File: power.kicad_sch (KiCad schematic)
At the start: 35 parts, among them J1 OBD-II harness, U1 TLV431A

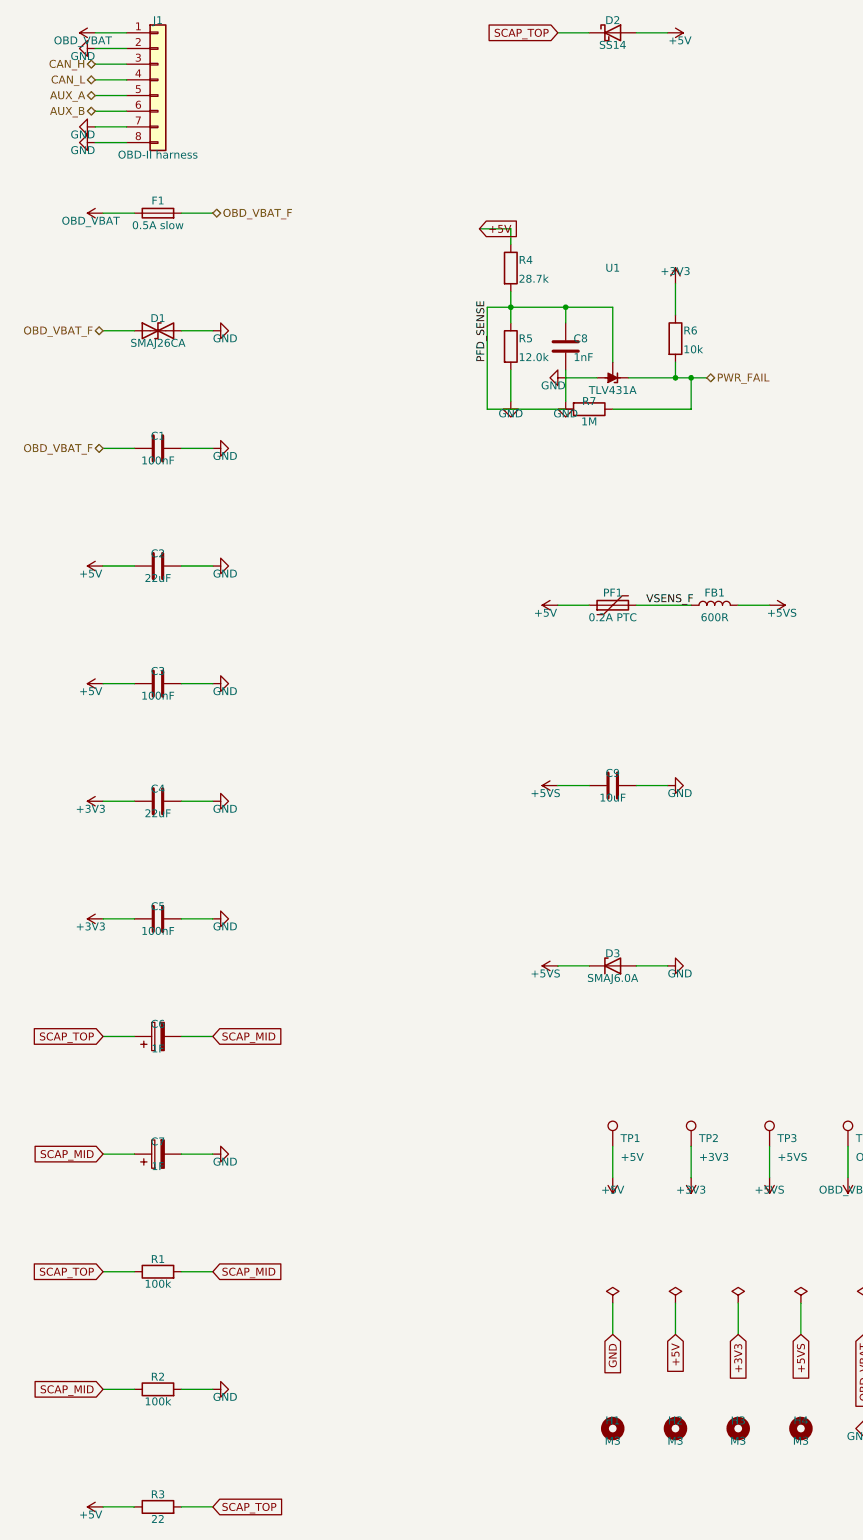
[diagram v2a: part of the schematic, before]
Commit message: Route, audit and document the carrier; verify every part number against the catalogue
Ordering is the point of this pass, so the part numbers came first. Every
LCSC number on the board was opened and read -- manufacturer part, package,
and the parameter that decides whether it is the right part. That found:

  C2148396 for the MCP2518FD    is an 18.7k resistor, out of stock -> C626759
  C255909  for a 40 MHz crystal is a 16 MHz crystal              -> C5186937
  C157966  for a JST PH 10-way  is a JST XH 9-way, 2.5 mm pitch  -> C158038

Three of the five numbers introduced last sitting were wrong, and all three
were plausible enough that the BOM exported clean. docs/PARTS.md records the
lot, including that LCSC's own listing for the microSD socket claims it has
no card-detect switch -- it has one, and the schematic is right.

Two footprints would not have soldered: both polyfuses are 1812 parts sitting
on a 1206 land, inherited from the parent board where nothing had ever
compared a part's package against its footprint. And the generic-passive
table was keyed on value alone, so the 1206 positions added last sitting
would have ordered 0805 parts -- right resistance, wrong footprint, every
board. It is keyed on (value, package) now and returns nothing rather than
guessing, so an unmatched line has no part number and somebody has to look.

Several values moved to match what is actually stocked: the power-fail
divider to 43k/18k (same trip point to 2 mV, both stocked 1 % parts), the
K-line series and pull-up to 20 R and 750 R, and the supercap charge resistor
from 22 R to 100 R -- 22 R put 1 W into a 250 mW part for the first several
seconds of every power-up.

Two real defects, both found by tools rather than by reading:

  - The hold-up Schottky was BACKWARDS. Reversed it shorts out the inrush
    limiter and blocks the discharge, so the supercap bank could never hold
    the rail up and the whole hold-up circuit was inert. audit_polarity found
    it once its expectat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
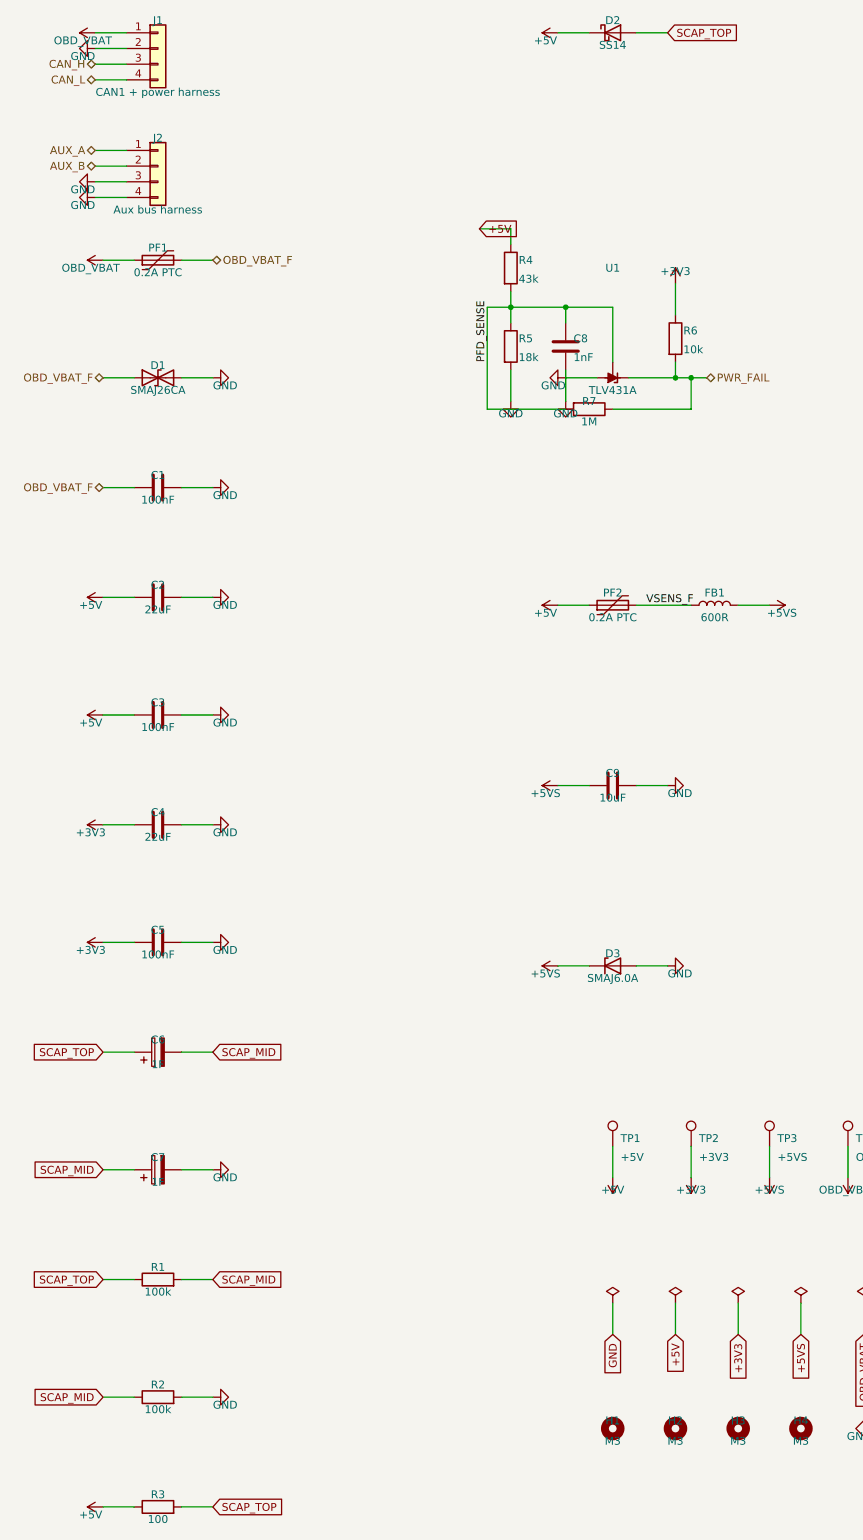
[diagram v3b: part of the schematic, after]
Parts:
- removed F1: 0.5A slow, Fuse:Fuse_1206_3216Metric, symbol Device:Fuse
- added J2: Aux bus harness, Connector_JST:JST_PH_B4B-PH-K_1x04_P2.00mm_Vertical, symbol Connector_Generic:Conn_01x04
- added PF2: 0.2A PTC, Resistor_SMD:R_1812_4532Metric, symbol Device:Polyfuse
- D2: Note Discharge path, bypassing the charge resistor. Anode on the bank: it conducts only once the rail has sagged a diode drop below the bank, which is exactly when the supply has gone away -> Discharge path, bypassing the charge resistor. Anode on the bank, cathode on the rail: it conducts only once the rail has sagged a diode drop below the bank, which is exactly when the supply has gone away
- J1: value OBD-II harness -> CAN1 + power harness; footprint Connector_JST:JST_PH_B8B-PH-K_1x08_P2.00mm_Vertical -> Connector_JST:JST_PH_B4B-PH-K_1x04_P2.00mm_Vertical; symbol Connector_Generic:Conn_01x08 -> Connector_Generic:Conn_01x04; MPN JST B8B-PH-K-S(LF)(SN) -> JST B4B-PH-K-S(LF)(SN); Note Pins 3/4 are the first CAN bus, always. Pins 5/6 are the se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 -> OBD-II pins 16/4/6/14. Pin 1 is sense only -- the board is 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
- PF1: footprint Resistor_SMD:R_1206_3216Metric -> Resistor_SMD:R_1812_4532Metric; MPN Bourns MF-MSMF020 -> Bourns MF-MSMF020/60-2; Note Resettable: a shorted sensor wire trips this, not the dev b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 -> OBD-II pin 16 is PERMANENT battery -- live with the ignitio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
- R3: value 22 -> 100; Note Inrush limit. 1206 for the pulse rating: 210 mA into 22 ohm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 -> Inrush limit, and the value is set by the resistor's own ra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
- R4: value 28.7k -> 43k
- R5: value 12.0k -> 18k; Note Lower leg: trips at 1.24V * 40.7/12.0 = 4.20V. The rail sit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 -> Lower leg: trips at 1.24V * 61/18 = 4.202V. The rail sits a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
- R7: Note Hysteresis, about 0.1 V at the rail. A USB rail is noisier 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 -> Hysteresis. The sense node sees 43k||18k = 12.7k, so 3.3 V 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
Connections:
- net +5V: now also D2.1 (K), PF2.1; no longer D2.2 (A), PF1.1
- net AUX_A: now also J2.1 (Pin_1); no longer J1.5 (Pin_5)
- net AUX_B: now also J2.2 (Pin_2); no longer J1.6 (Pin_6)
- net GND: now also J2.3 (Pin_3), J2.4 (Pin_4); no longer J1.7 (Pin_7), J1.8 (Pin_8)
- net OBD_VBAT: now also PF1.1
- net OBD_VBAT_F: now also PF1.2
- net SCAP_TOP: now also D2.2 (A); no longer D2.1 (K)
- net VSENS_F: now also PF2.2; no longer PF1.2
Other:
- moved on the sheet: C1, C2, C3, C4, C5, C6, C7, D1, PF1, R1, R2

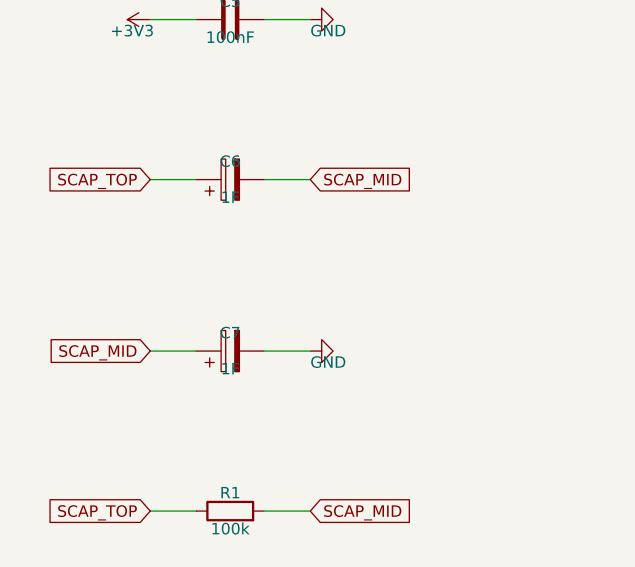
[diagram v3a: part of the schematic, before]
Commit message: Implement the cost reductions: 1% dividers and a 0.33 F bank -- $18.29 to $13.87
Two of the three changes from docs/COST.md. The third was dropped once I
checked it properly, which is the more interesting half of this commit.

PRECISION RESISTORS TO 1%, saving $2.62 measured. Fifteen 0.1% parts cost
$2.68 -- more than the CAN controller -- to tighten a divider whose error the
ADS1115's own +/-0.30% gain spec already dominates. Absolute scale has to be
calibrated whatever the tolerance, and the thing calibration cannot fix, the
match between the signal chain and the return attenuator, is fine at 1%: a
300 mV chassis offset leaves 6 mV instead of 0.6 mV, both negligible against
the 300 mV being removed.

The lower leg went 2.21k -> 2.2k with it, because E96 values do not exist in
the 1% jellybean library. That is a happy accident: 2.2/13.2 is exactly 1/6,
so DIVIDER_GAIN is a round 6.0000 instead of 5.9774.

HOLD-UP BANK 1 F -> 0.33 F per cell, saving roughly $1.80. 1 F bought 2500 ms
that nothing needs -- the parent board shipped 127 ms and that was judged
adequate, a healthy card flushes in 18 ms, and the worst stall the firmware
studies model is 500 ms. 0.33 F gives 825 ms shed, six times the parent's
margin and still 65% clear of that worst case. The budgets in fwsim, studies
11 and 12 and their sweep ranges all move with it.

THE microSD SWAP IS NOT DONE, and the $1.06 I quoted for it was arithmetic
against a part I could not verify. Those $0.04 sockets are house parts whose
only drawing is a scanned PDF with no extractable dimensions, so the land
pattern cannot be checked -- and shipping an unverified footprint on five
boards to save a dollar is not a trade this project should make. The
verifiable alternatives are worse than the search suggested: the Molex
47219-2001 with a KiCad footprint is $0.63 against the Hirose's $1.12, so the
honest saving is $0.49, and it costs the card-detect signal and swaps a
push-pull for a hinged lid. The Hirose stays. COST.md recor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
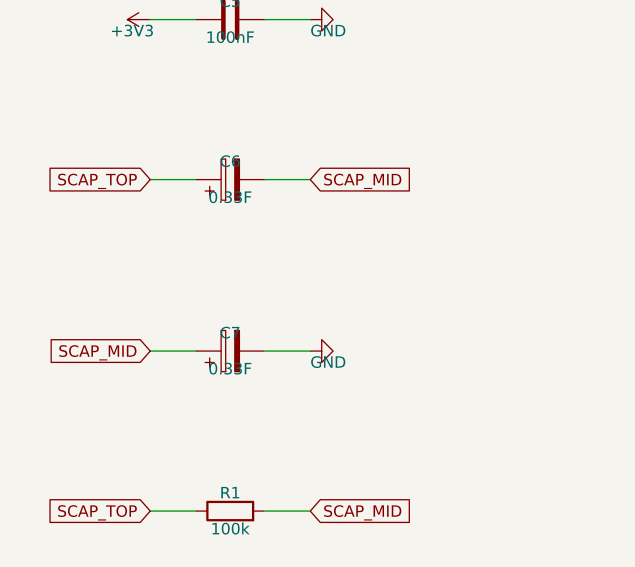
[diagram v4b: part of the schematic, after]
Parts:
- C6: value 1F -> 0.33F; Note Hold-up cell 1 of 2 in series -> 0.5 F at 5.4 V. Anything f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 -> Hold-up cell 1 of 2 in series -> 0.165 F at 5.4 V, which is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
- C7: value 1F -> 0.33F; Note Hold-up cell 2 of 2 in series -> 0.5 F at 5.4 V. Anything f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 -> Hold-up cell 2 of 2 in series -> 0.165 F at 5.4 V, which is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
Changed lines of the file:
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@@
       (effects (font (size 1.27 1.27)) )
     )
-    (property "Value" "1F" (at 36.83 184.88 270)
+    (property "Value" "0.33F" (at 36.83 184.88 270)
       (effects (font (size 1.27 1.27)) )
     )
@@
       (effects (font (size 1.27 1.27)) hide)
     )
-    (property "Note" "Hold-up cell 1 of 2 in series -> 0.5 F at 5.4 V. Anything from 0.1 F up works; 0.1 F still gives 500 ms. ESR must be under about 1 ohm -- check it, coin-type EDLCs are 30-200 ohm and will not work here" (at 36.83 184.88 270)
+    (property "Note" "Hold-up cell 1 of 2 in series -> 0.165 F at 5.4 V, which is 825 ms with the strip shed. 1 F was the first pick and bought 2500 ms that nothing needs: the parent board shipped 127 ms and that was judged adequate, a healthy card flushes in 18 ms, and the worst stall gen/simulate_firmware.py models is 500 ms. This is still six times the parent's margin and it is the most expensive line on the board -- see docs/COST.md. ESR must be under about 1 ohm; cylindrical cells are around 200 mohm, coin-type EDLCs are 30-200 OHM and will not work here" (at 36.83 184.88 270)
       (effects (font (size 1.27 1.27)) hide)
     )
@@
       (effects (font (size 1.27 1.27)) )
     )
-    (property "Value" "1F" (at 36.83 203.93 270)
+    (property "Value" "0.33F" (at 36.83 203.93 270)
       (effects (font (size 1.27 1.27)) )
     )
@@
       (effects (font (size 1.27 1.27)) hide)
     )
-    (property "Note" "Hold-up cell 2 of 2 in series -> 0.5 F at 5.4 V. Anything from 0.1 F up works; 0.1 F still gives 500 ms. ESR must be under about 1 ohm -- check it, coin-type EDLCs are 30-200 ohm and will not work here" (at 36.83 203.93 270)
+    (property "Note" "Hold-up cell 2 of 2 in series -> 0.165 F at 5.4 V, which is 825 ms with the strip shed. 1 F was the first pick and bought 2500 ms that nothing needs: the parent board shipped 127 ms and that was judged adequate, a healthy card flushes in 18 ms, and the worst stall gen/simulate_firmware.py models is 500 ms. This is still six times the parent's margin and it is the most expensive line on the board -- see docs/COST.md. ESR must be under about 1 ohm; cylindrical cells are around 200 mohm, coin-type EDLCs are 30-200 OHM and will not work here" (at 36.83 203.93 270)
       (effects (font (size 1.27 1.27)) hide)
     )
